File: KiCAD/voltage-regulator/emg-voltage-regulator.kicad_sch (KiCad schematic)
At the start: 15 parts, among them J1 Conn_01x03_Male, U1 MAX764ESA+

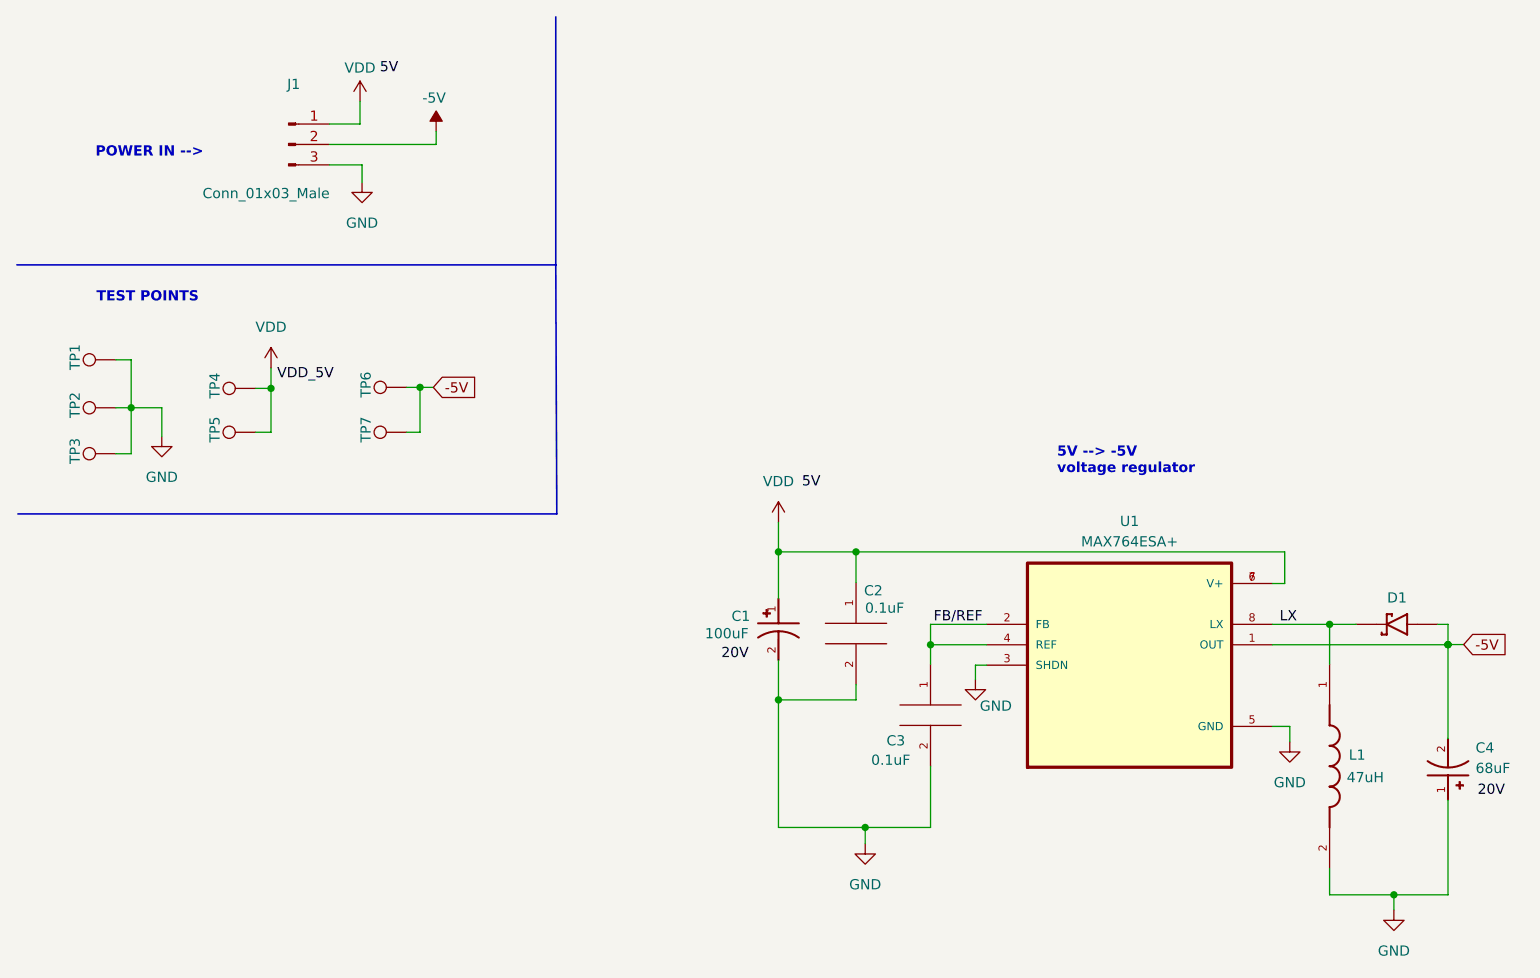
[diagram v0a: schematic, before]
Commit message: layout for voltage regulator done
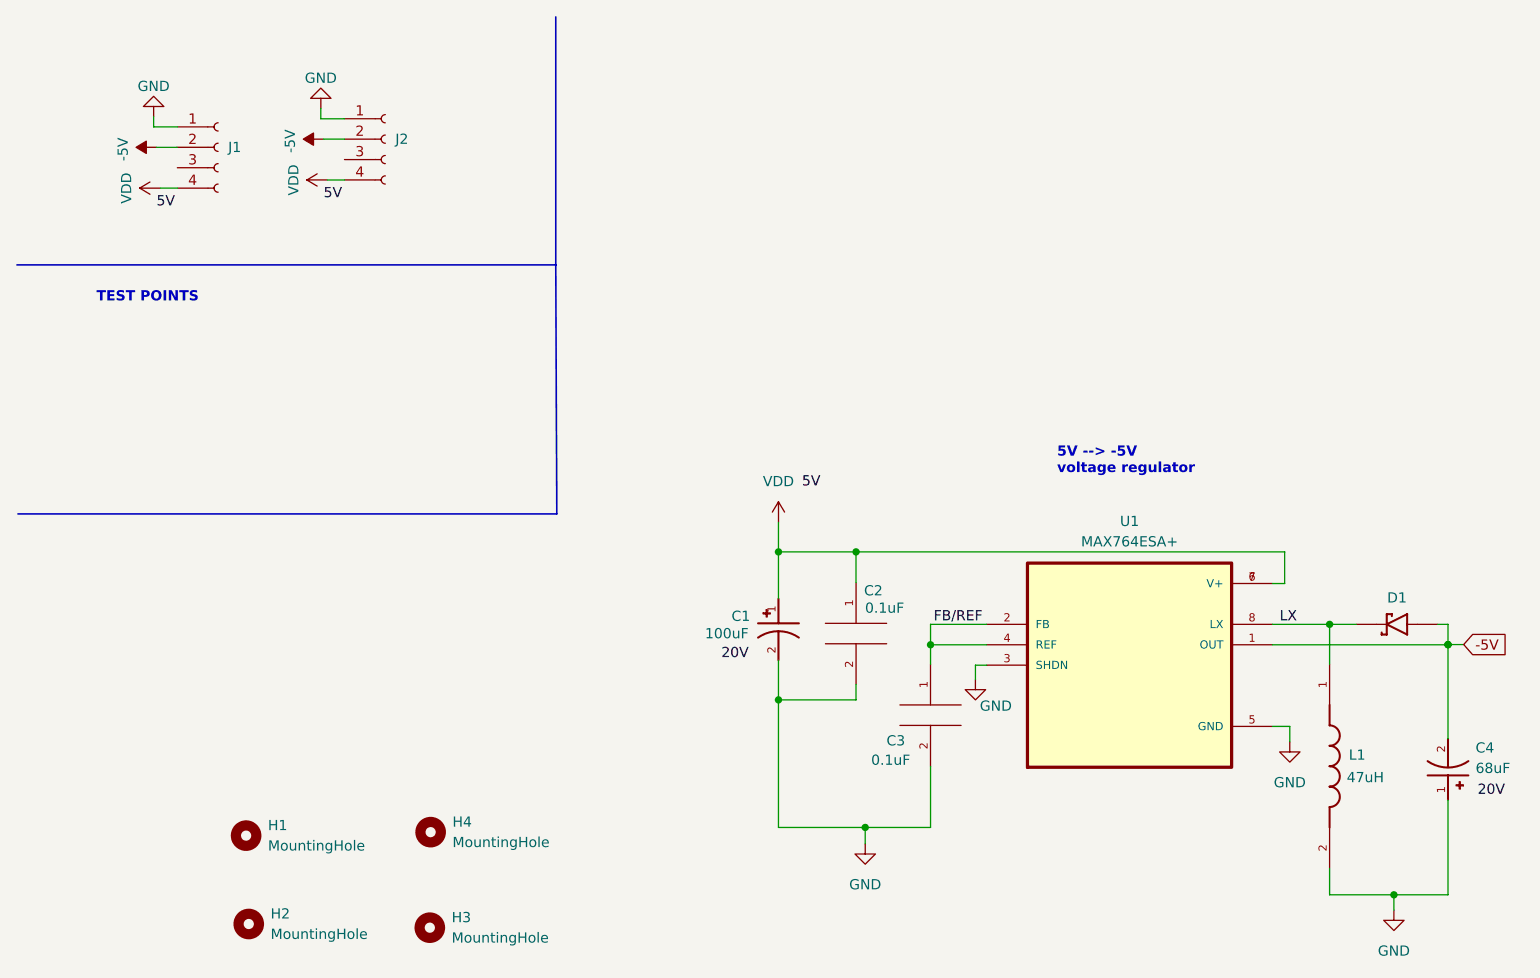
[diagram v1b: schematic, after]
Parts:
- removed J1: Conn_01x03_Male, Connector_PinHeader_2.54mm:PinHeader_1x03_P2.54mm_Vertical, symbol Connector:Conn_01x03_Male
- removed TP1, TP2, TP3, TP4, TP5, TP6, TP7: TestPoint, TestPoint:TestPoint_Pad_1.0x1.0mm, symbol Connector:TestPoint
- added H1, H2, H3, H4: MountingHole, MountingHole:MountingHole_2.2mm_M2, symbol Mechanical:MountingHole
- added J1, J2: Conn_01x04_Female, Connector_PinHeader_1.27mm:PinHeader_1x04_P1.27mm_Vertical, symbol Connector:Conn_01x04_Female
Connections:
- net -5V: now also J1.2 (Pin_2), J2.2 (Pin_2)
- net GND: now also J1.1 (Pin_1), J2.1 (Pin_1)
- net VDD: now also J1.4 (Pin_4), J2.4 (Pin_4)
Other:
- note removed: "POWER IN -->"
